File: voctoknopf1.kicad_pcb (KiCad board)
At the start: 2 copper layers, 0 parts

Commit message: scematic + netlist
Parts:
- added ARDUINO1: ARDUINO_NANO, Modules:Arduino_Nano_WithMountingHoles, F.Cu at (0.00, 0.00)
- added ARDUINO2: Nano Ethernet Shield, Modules:Arduino_Nano_WithMountingHoles, F.Cu at (0.00, 0.00)
- added D1, D2: LED, LEDs:LED_D5.0mm, F.Cu at (85.0, 50.8)
- added R1, R10, R12, R14, R16, R18, R20, R22, R24, R27, R3, R5, R7, R8: 220, Resistors_THT:R_Axial_DIN0207_L6.3mm_D2.5mm_P7.62mm_Horizontal, F.Cu at (85.0, 50.8)
- added R11, R13, R15, R17, R19, R2, R21, R23, R25, R26, R4, R6, R9: 10 k, Resistors_THT:R_Axial_DIN0207_L6.3mm_D2.5mm_P7.62mm_Horizontal, F.Cu at (85.0, 50.8)
- added SW1, SW10, SW11, SW12, SW2, SW3, SW4, SW5, SW6, SW7, SW8, SW9: MX_D, cherry:SW_PCB_4PIN, F.Cu at (85.0, 50.8)
- added U1, U2: MCP23017, Housings_DIP:DIP-28_W7.62mm_LongPads, F.Cu at (85.0, 50.8)
- added U3: CPC1017N, Buttons_Switches_SMD:SW_DIP_x2_W8.61mm_Slide_LowProfile, F.Cu at (85.0, 50.8)
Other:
- net class Default: clearance 0.2 -> 0.25
- rule trace_clearance: 0.2 -> 0.25

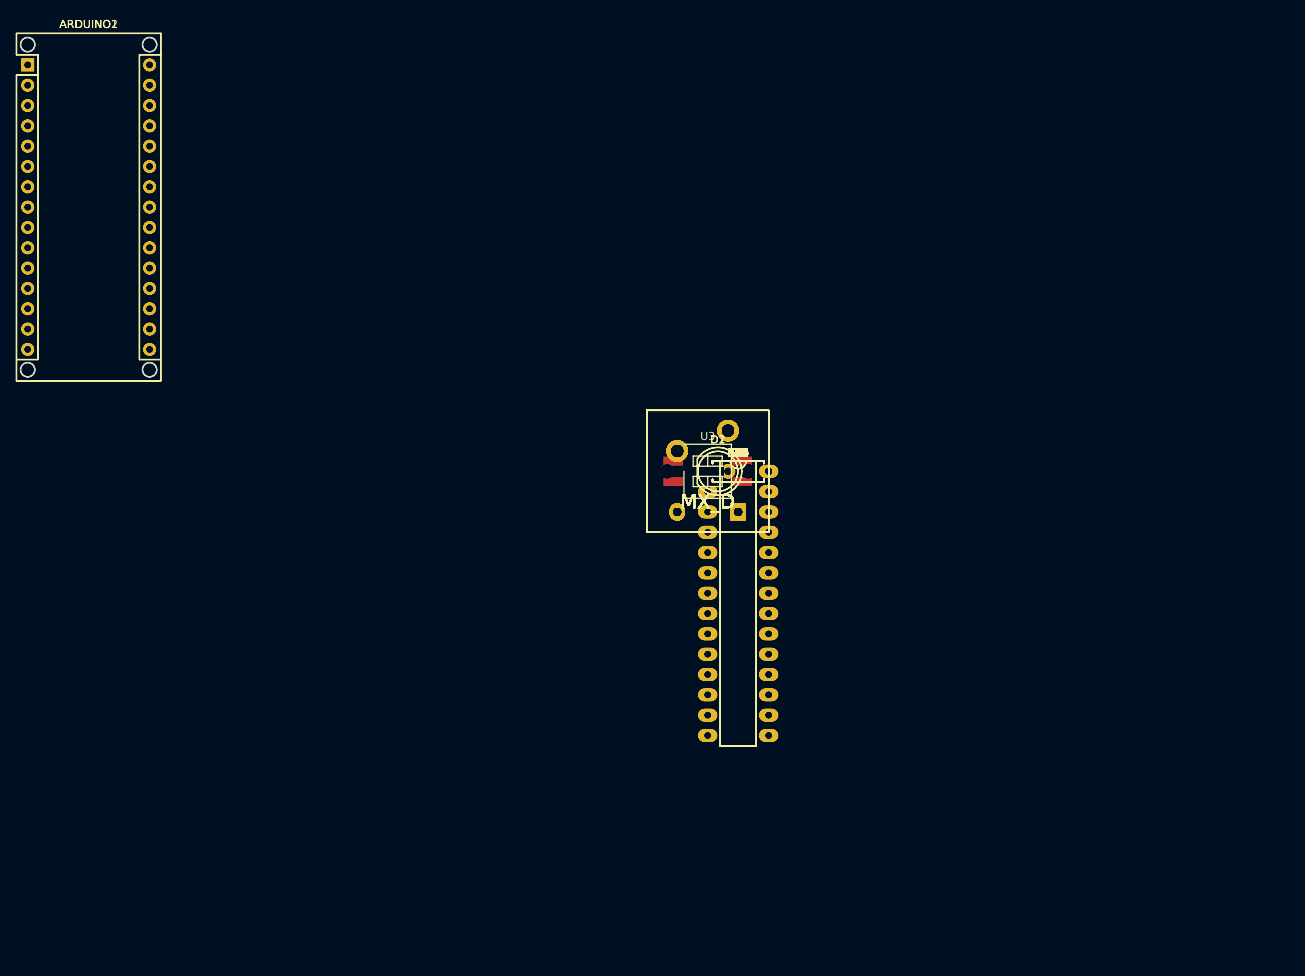
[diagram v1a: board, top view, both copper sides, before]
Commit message: sorting components on pcb
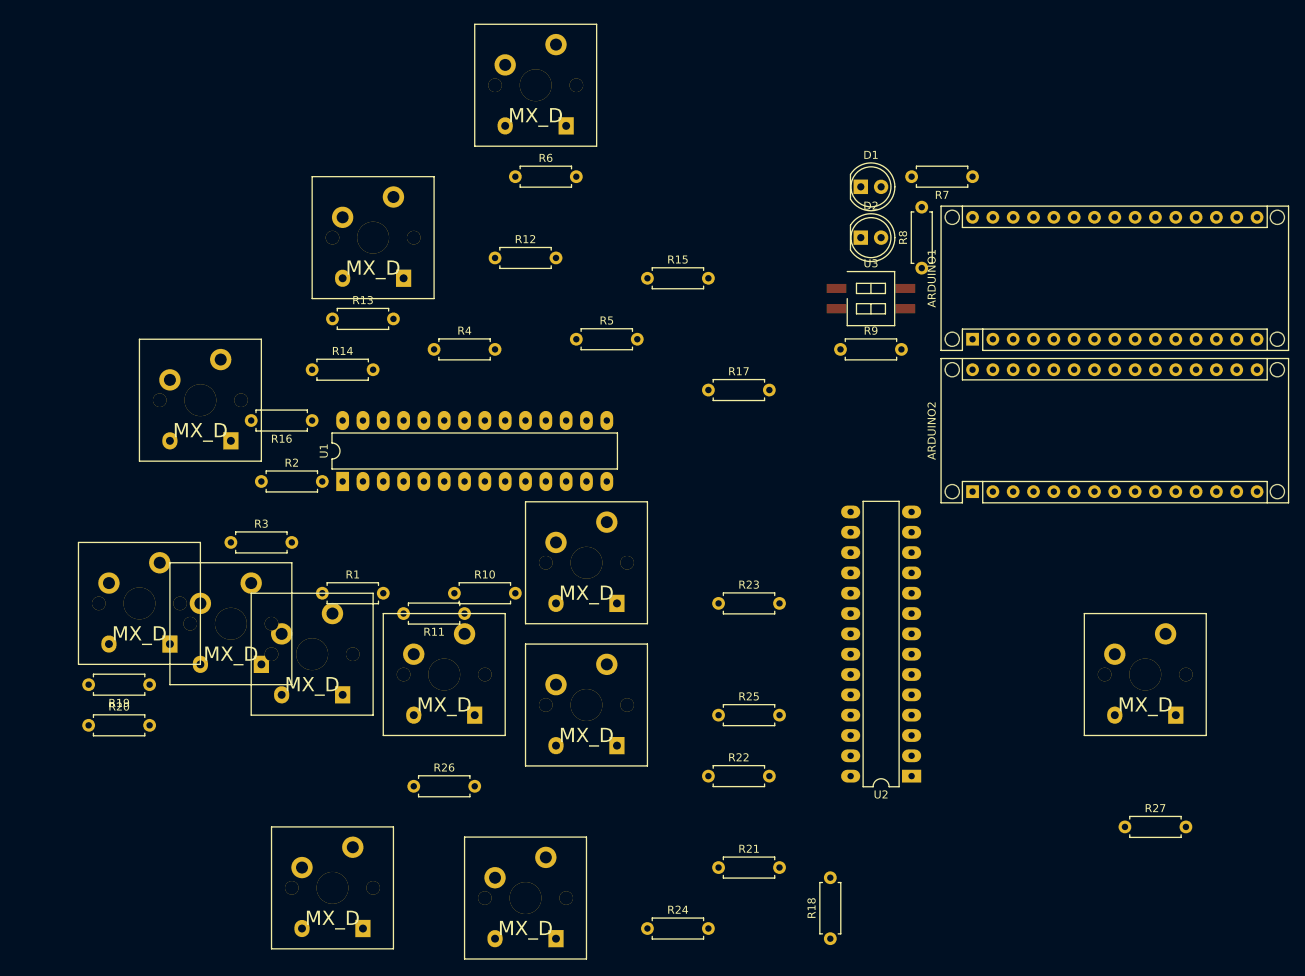
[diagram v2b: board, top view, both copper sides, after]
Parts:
- moved ARDUINO2 129.6 mm to (118.1, 53.3), turned to 90 degrees
- moved ARDUINO1 123.0 mm to (118.1, 34.3), turned to 90 degrees
- moved R20 83.6 mm to (7.62, 82.5)
- moved R19 74.7 mm to (15.2, 77.5), turned to 180 degrees
- moved SW9 72.9 mm to (14.0, 67.3)
- moved SW11 70.1 mm to (38.1, 102.9)
- moved R27 68.5 mm to (137.2, 95.2)
- moved SW7 64.0 mm to (21.6, 41.9)
- moved SW2 62.6 mm to (25.4, 69.8)
- moved R18 60.4 mm to (100.3, 109.2), turned to 90 degrees
- moved SW12 60.3 mm to (139.7, 76.2)
- moved R3 60.3 mm to (25.4, 59.7)
- moved SW10 58.0 mm to (62.2, 104.1)
- moved R24 57.6 mm to (77.5, 108.0)
- moved R2 55.8 mm to (29.2, 52.1)
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
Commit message: pcb work
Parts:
- added G***: LOGO, library:Untitled10, F.Cu at (86.0, 56.5)
- moved R26 98.9 mm to (143.5, 63.5), turned to 180 degrees
- moved SW7 80.5 mm to (100.5, 57.8)
- moved R18 75.6 mm to (34.3, 72.4), turned to 270 degrees
- moved SW5 61.4 mm to (44.5, 61.0)
- moved SW1 61.4 mm to (26.7, 20.3)
- moved SW2 56.3 mm to (52.1, 20.3)
- moved R16 54.6 mm to (90.0, 40.5), turned to 270 degrees
- moved SW11 53.4 mm to (85.1, 77.5)
- moved R3 52.1 mm to (61.0, 21.6)
- moved SW3 50.0 mm to (96.2, 19.8)
- moved R21 49.9 mm to (38.1, 87.6)
- moved R20 48.1 mm to (54.6, 72.4), turned to 270 degrees
- moved R6 47.8 mm to (108.5, 18.5), turned to 90 degrees
- moved SW8 45.8 mm to (24.1, 77.5)
- moved SW6 44.9 mm to (64.8, 61.0)
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
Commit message: pbc work
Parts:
- moved R3 14.8 mm to (75.8, 22.0)
- moved R4 14.4 mm to (75.2, 15.8)
- moved SW2 9.95 mm to (62.0, 19.8)
- moved R17 8.07 mm to (96.0, 48.0), turned to 90 degrees
- moved R9 6.58 mm to (131.5, 10.5), turned to 0 degrees
- moved R2 5.96 mm to (41.2, 16.0)
- moved R1 5.69 mm to (41.0, 23.2)
- moved D2 2.50 mm to (122.8, 30.0), turned to 90 degrees
- moved SW1 1.22 mm to (27.8, 19.8)
- moved U3 0.35 mm to (122.8, 12.2)

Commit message: last saved November 2017
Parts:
- moved G*** 111.3 mm to (89.2, -54.8)
- moved SW11 24.8 mm to (104.0, 93.5)
- moved SW10 21.1 mm to (78.5, 93.5)
- moved R20 19.3 mm to (65.2, 88.5)
- moved SW9 18.3 mm to (52.8, 93.8)
- moved R22 18.2 mm to (91.0, 88.5), turned to 270 degrees
- moved R24 17.0 mm to (113.5, 80.8), turned to 180 degrees
- moved R15 16.8 mm to (91.0, 64.5)
- moved SW8 16.5 mm to (27.0, 93.8)
- moved R18 16.4 mm to (40.0, 87.8)
- moved R23 16.1 mm to (75.5, 80.8)
- moved R14 15.8 mm to (75.0, 56.8)
- moved SW6 15.4 mm to (78.5, 68.0)
- moved R1 15.2 mm to (52.2, 33.5), turned to 180 degrees
- moved R25 14.5 mm to (95.5, 81.0)
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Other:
- board outline added: 161.2 x 88.5 mm
